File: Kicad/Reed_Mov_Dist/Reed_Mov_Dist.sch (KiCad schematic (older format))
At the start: 21 parts, among them J1 Barrel_Jack, J10 HC-SRO4, J11 URM37, J12 LV-MaxSonar-EZ1, J2 Conn_01x02, J3 Conn_01x02, J4 Conn_01x02, J5 LIS3DH_1, J6 ITG3200, J7 LIS3DH_2, J8 TTL_Level_Shifter_1, J9 TTL_Level_Shifter_2, U1 LM7805_TO220, U2 XBEE

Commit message: Corrected distance sensors bug. Added jumper to enable or disable Xbee, to access arduino pro mini serial port.
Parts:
- added J13: Conn_01x02, Socket_Strips:Socket_Strip_Straight_1x02_Pitch2.54mm, symbol Conn_01x02
- uP1: symbol ARDUPROMINI-6 -> ARDUPROMINI-6-RESCUE-Reed_Mov_Dist
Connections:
- net labels added: 3V3_Xbee
- wire segments 88 -> 90
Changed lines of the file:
@@
 EESchema Schematic File Version 2
+LIBS:Reed_Mov_Dist-rescue
 LIBS:power
 LIBS:device
@@
 LIBS:freetronics_schematic
 LIBS:ArduProMiniTKB
-LIBS:lis3dh
 LIBS:agg-kicad
 LIBS:Reed_Mov_Dist-cache
@@
 $EndDescr
 $Comp
-L ARDUPROMINI-6 uP1
+L ARDUPROMINI-6-RESCUE-Reed_Mov_Dist uP1
 U 1 1 5A1D41F9
 P 5600 4450
@@
 NoConn ~ 5750 1800
 NoConn ~ 5750 1700
+Text GLabel 9600 5300 2    60   Input ~ 0
+TRIG_HC_HV
 Text GLabel 9600 5400 2    60   Input ~ 0
-TRIG_HC_HV
-Text GLabel 9600 5300 2    60   Input ~ 0
 ECHO_HC_HV
+Text GLabel 9600 5500 2    60   Input ~ 0
+TRIG_URM_HV
 Text GLabel 9600 5600 2    60   Input ~ 0
-TRIG_URM_HV
-Text GLabel 9600 5500 2    60   Input ~ 0
 ECHO_URM_HV
 Text GLabel 8600 5300 0    60   Input ~ 0
@@
 $EndComp
 Text GLabel 1300 6350 0    60   Input ~ 0
-3V3
+3V3_Xbee
 Text GLabel 1300 7250 0    60   Input ~ 0
 GND
@@
 	5600 6150 5700 6150
 NoConn ~ 5600 6450
+Text GLabel 1100 5750 2    60   Input ~ 0
+3V3_Xbee
+Wire Wire Line
+	1100 5900 1100 5750
+Text GLabel 1000 5750 0    60   Input ~ 0
+3V3
+Wire Wire Line
+	1000 5750 1000 5900
+$Comp
+L Conn_01x02 J13
+U 1 1 5A1F6CFC
+P 1100 6100
+F 0 "J13" H 1100 6200 50  0000 C CNN
+F 1 "Conn_01x02" H 1100 5900 50  0000 C CNN
+F 2 "Socket_Strips:Socket_Strip_Straight_1x02_Pitch2.54mm" H 1100 6100 50  0001 C CNN
+F 3 "" H 1100 6100 50  0001 C CNN
+	1    1100 6100
+	0    1    1    0
+$EndComp
 $EndSCHEMATC

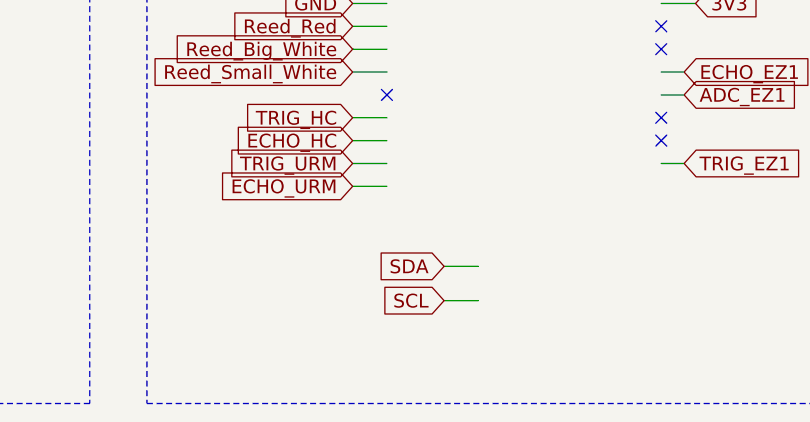
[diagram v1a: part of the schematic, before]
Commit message: Corrected SDA and SCL switched bug.
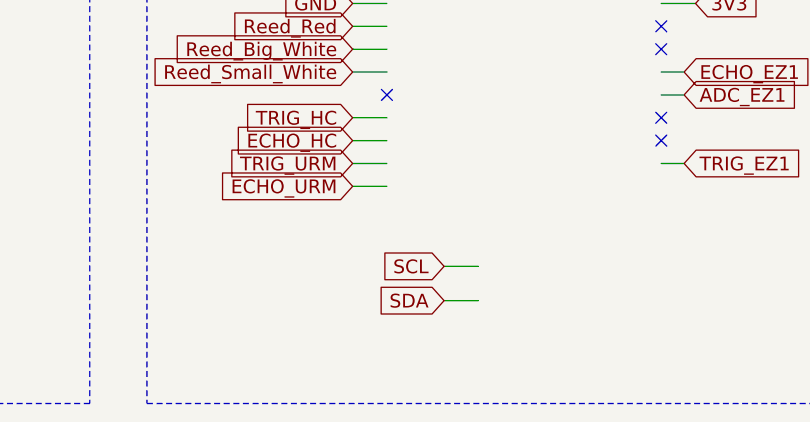
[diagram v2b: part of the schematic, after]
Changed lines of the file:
@@
 	-1   0    0    1
 $EndComp
+Text GLabel 4650 7150 0    60   Input ~ 0
+SDA
 Text GLabel 4650 7000 0    60   Input ~ 0
-SDA
-Text GLabel 4650 7150 0    60   Input ~ 0
 SCL
 $Comp
